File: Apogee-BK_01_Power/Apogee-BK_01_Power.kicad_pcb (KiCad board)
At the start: 2 copper layers, 87.5 x 46.2 mm, 12 parts, among them J1 Power In (+12VDC), J2 Power Out, U1 PSU5, U2 R-78CK5.0-0.5

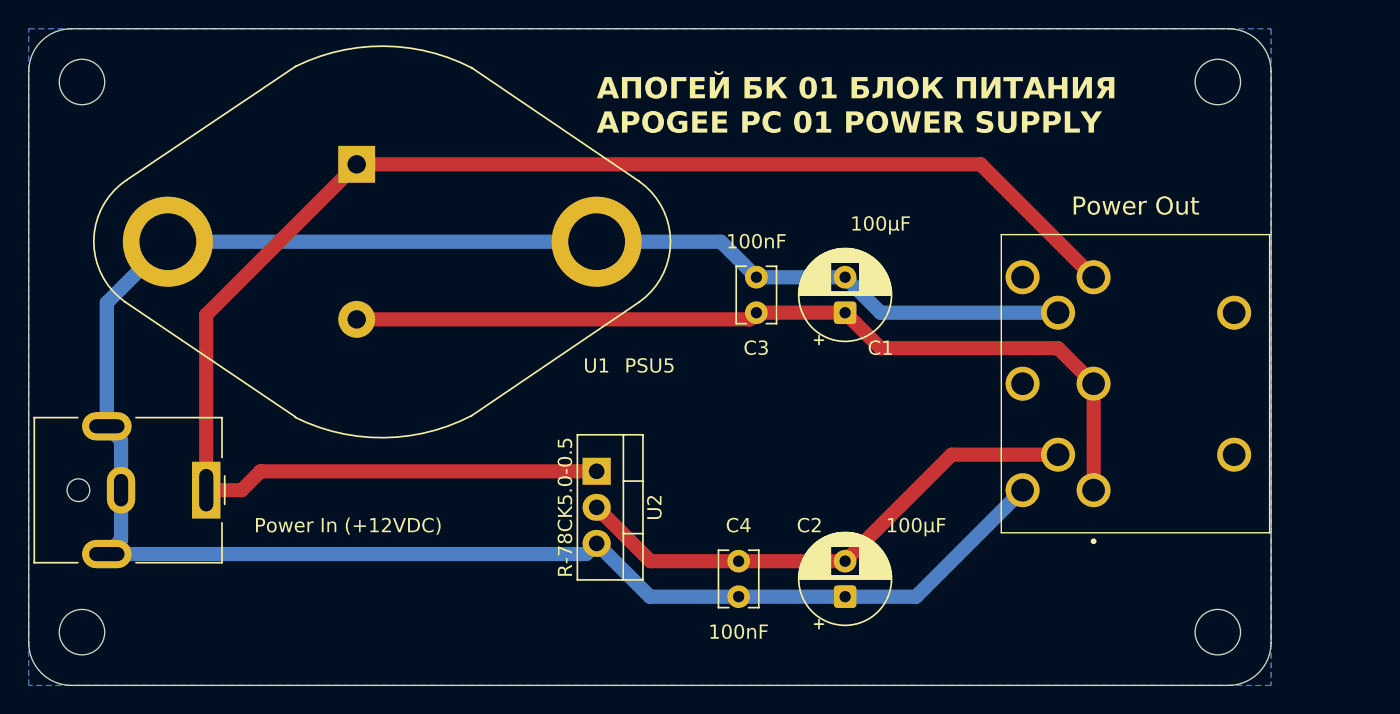
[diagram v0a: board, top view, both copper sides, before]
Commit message: Added fuse to 12V input rail
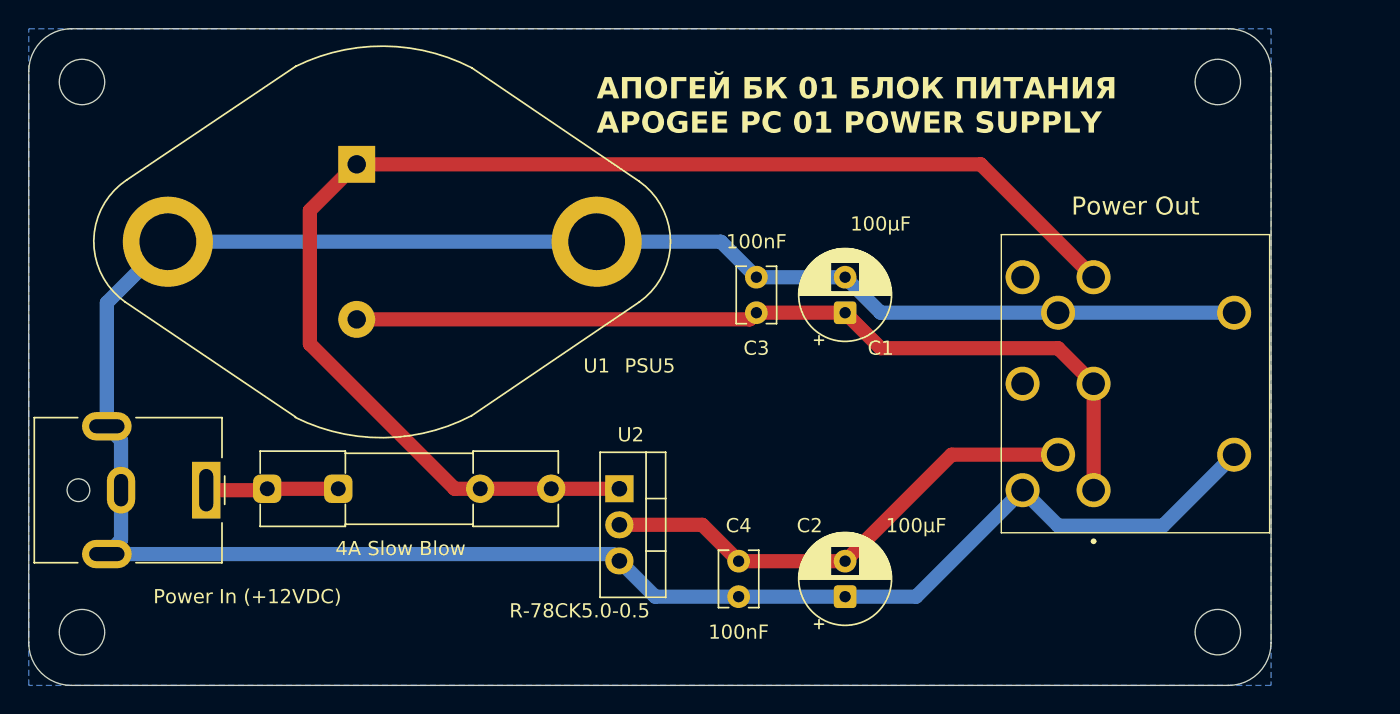
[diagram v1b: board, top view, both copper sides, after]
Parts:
- added F1: Fuse, Fuse:Fuseholder_Clip-5x20mm_Littelfuse_111_Inline_P20.00x5.00mm_D1.05mm_Horizontal, F.Cu at (121.8, 92.4)
- moved U2 2.02 mm to (146.6, 92.4)
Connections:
- J1 pad 1: /+12V -> /+12V_{IN}
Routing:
- net /GND: track 158.9 -> 188.6 mm
- net /+12V: track 110.6 -> 95.3 mm
- net /+12V_{IN}: track 0.00 -> 9.34 mm
- net /-5V: track 37.2 -> 35.1 mm
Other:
- board text added: "4A Slow Blow"
